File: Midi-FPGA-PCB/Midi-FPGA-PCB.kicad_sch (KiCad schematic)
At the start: 13 parts, among them Q1 DMP2123L, SW1 SW_Push, U1 ESP32-WROOM-32, U2 AP7361EA

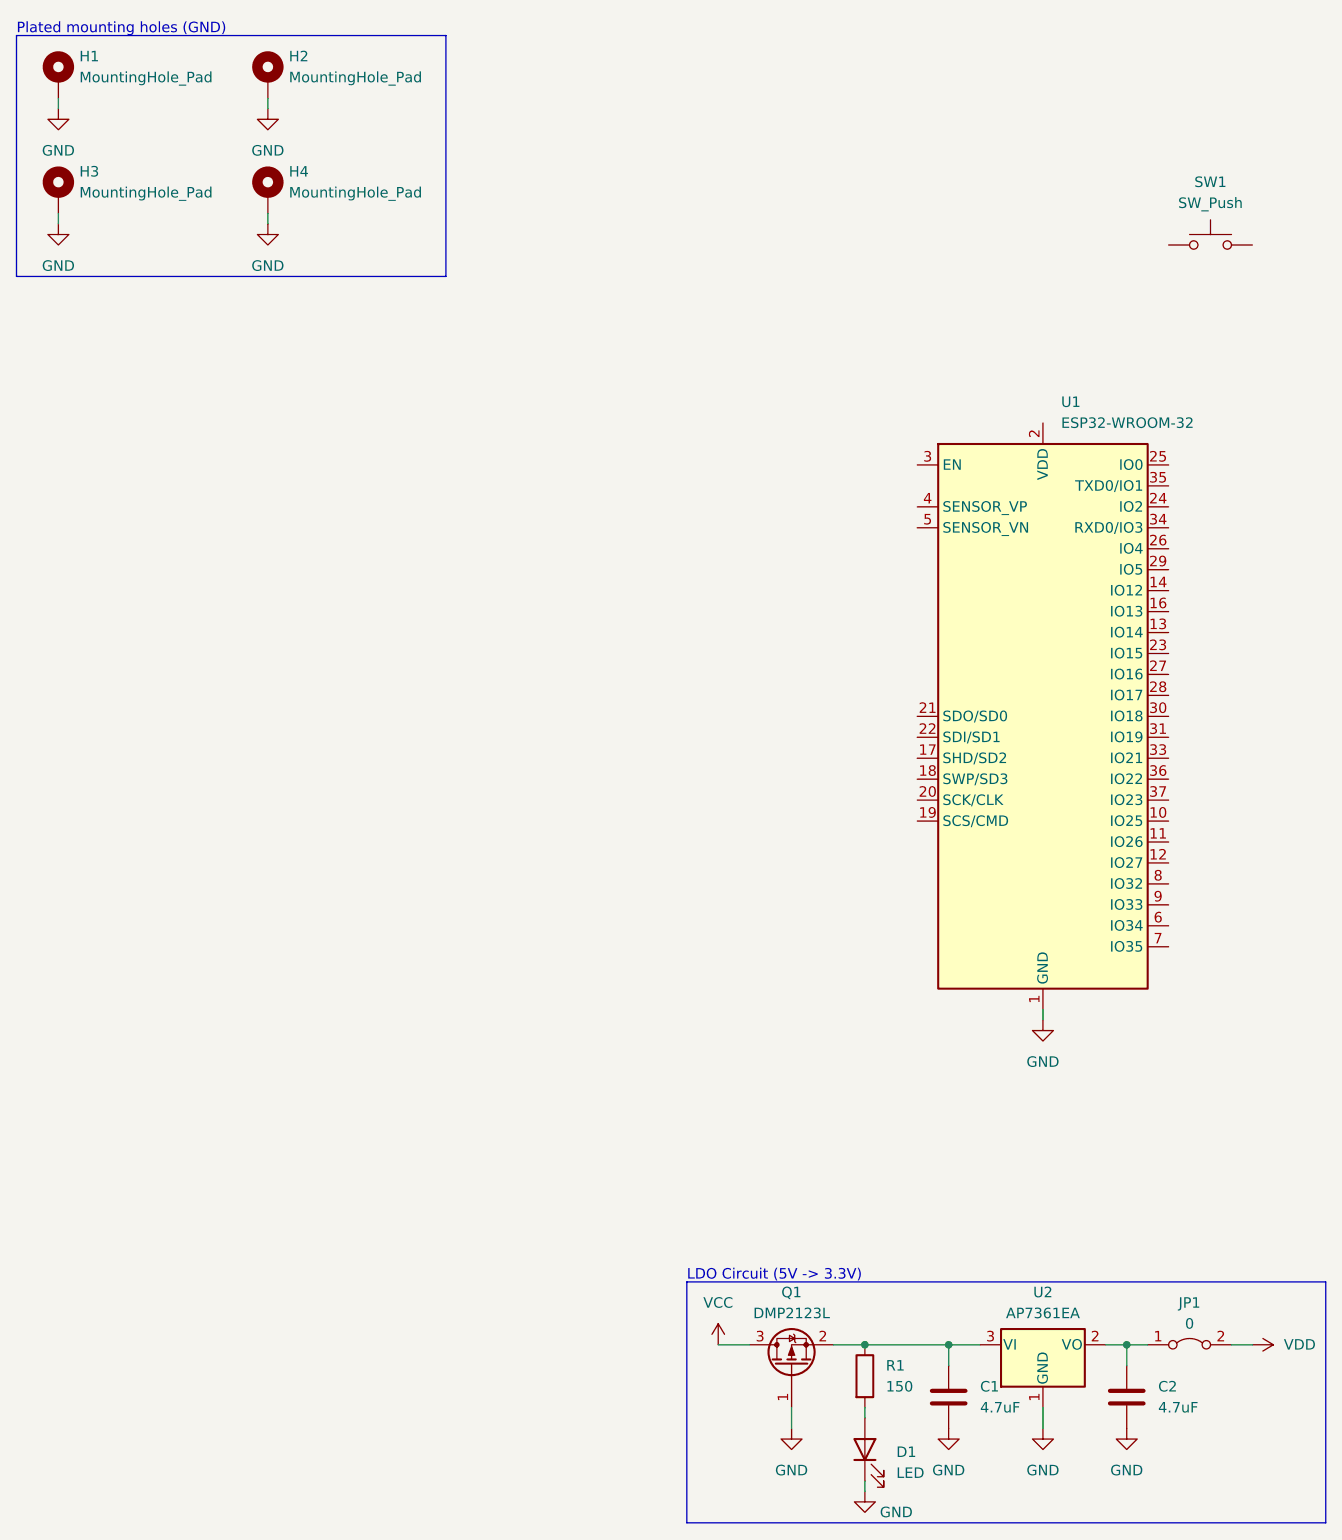
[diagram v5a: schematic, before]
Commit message: Created enable circuit
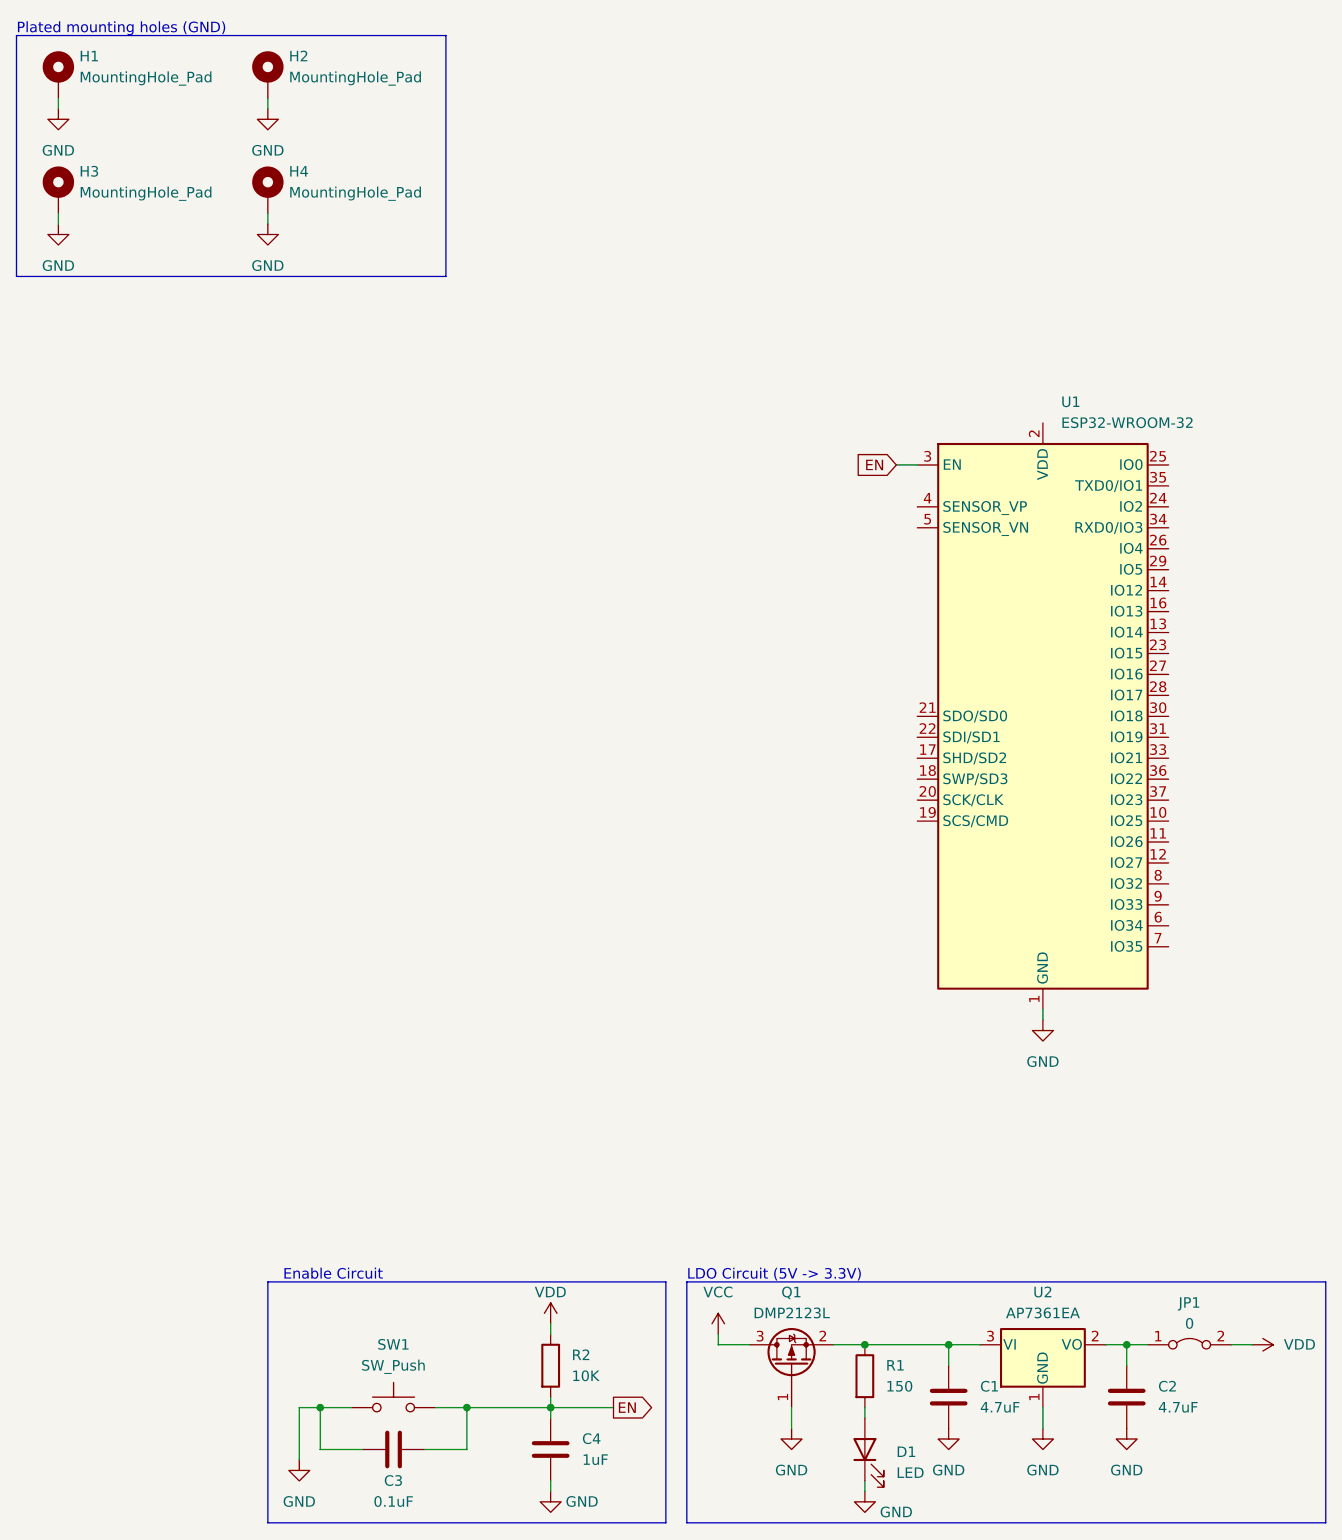
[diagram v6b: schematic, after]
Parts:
- added C3: 0.1uF, Capacitor_SMD:C_0805_2012Metric_Pad1.18x1.45mm_HandSolder, symbol Device:C
- added C4: 1uF, Capacitor_SMD:C_0805_2012Metric_Pad1.18x1.45mm_HandSolder, symbol Device:C
- added R2: 10K, Resistor_SMD:R_0805_2012Metric_Pad1.20x1.40mm_HandSolder, symbol Device:R
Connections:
- net GND: now also SW1.1, C3.1, C4.2
- net VDD: now also R2.1
- net EN: now reaches SW1.2
- net EN: now also U1.3 (EN), C3.2, C4.1, R2.2
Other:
- note added: "Enable Circuit"
- moved on the sheet: SW1

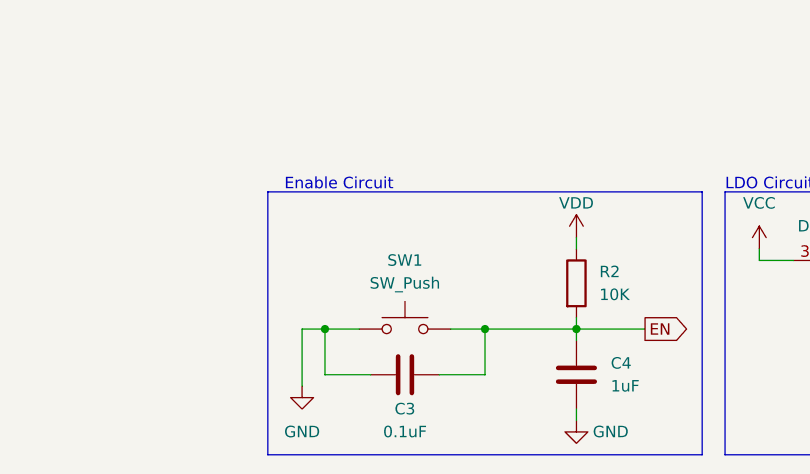
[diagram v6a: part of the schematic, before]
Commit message: Named reset switch
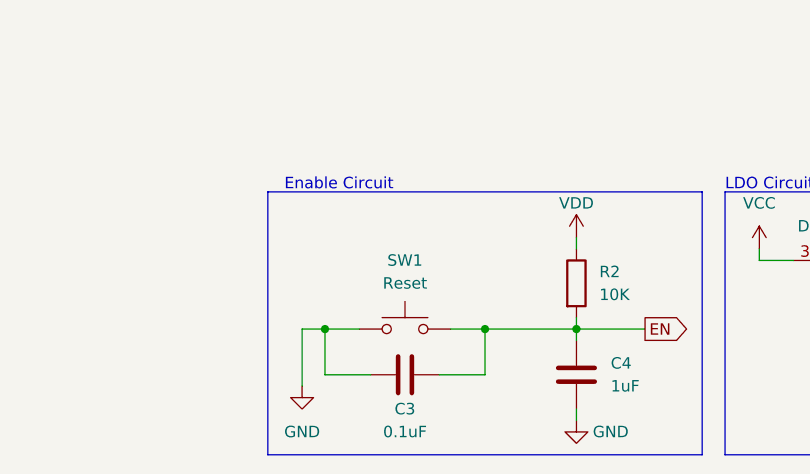
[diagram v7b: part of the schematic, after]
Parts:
- SW1: value SW_Push -> Reset
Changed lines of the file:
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@@
       (effects (font (size 1.27 1.27)))
     )
-    (property "Value" "SW_Push" (at 60.96 176.53 0)
+    (property "Value" "Reset" (at 60.96 176.53 0)
       (effects (font (size 1.27 1.27)))
     )

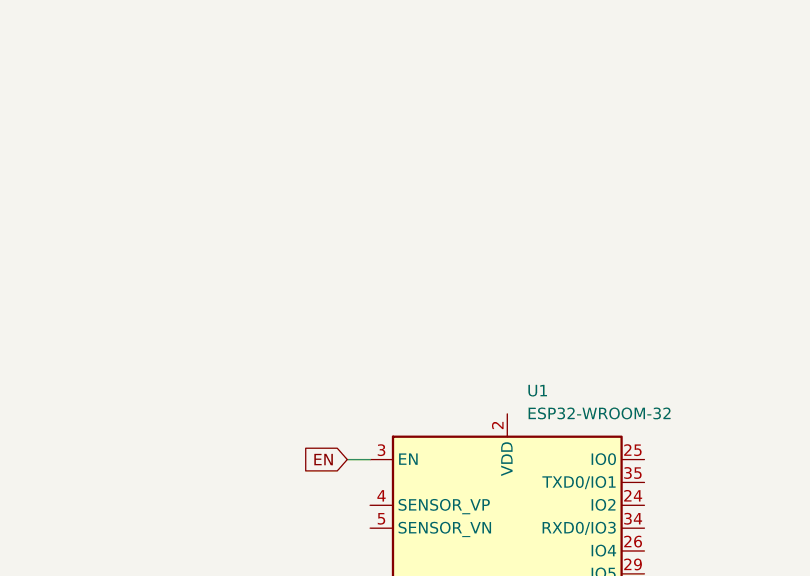
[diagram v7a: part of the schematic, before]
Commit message: Finished power and enable circuitry
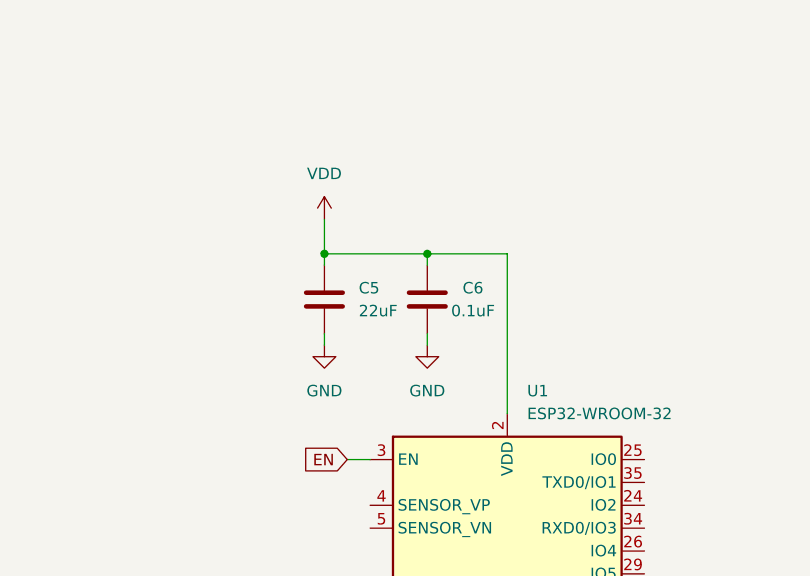
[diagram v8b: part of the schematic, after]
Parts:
- added C5: 22uF, Capacitor_SMD:C_0805_2012Metric_Pad1.18x1.45mm_HandSolder, symbol Device:C
- added C6: 0.1uF, Capacitor_SMD:C_0805_2012Metric_Pad1.18x1.45mm_HandSolder, symbol Device:C
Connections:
- net GND: now also C5.2, C6.1
- net VDD: now also U1.2 (VDD), C5.1, C6.2
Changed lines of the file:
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@@
   (junction (at 52.07 181.61) (diameter 0) (color 0 0 0 0)
   )
+  (junction (at 130.81 44.45) (diameter 0) (color 0 0 0 0)
+  )
   (junction (at 80.01 181.61) (diameter 0) (color 0 0 0 0)
   )
+  (junction (at 119.38 44.45) (diameter 0) (color 0 0 0 0)
+  )
   (junction (at 149.86 173.99) (diameter 0) (color 0 0 0 0)
   )
@@
     (stroke (width 0) (type default))
   )
+  (wire (pts (xy 119.38 44.45) (xy 130.81 44.45))
+    (stroke (width 0) (type default))
+  )
+  (wire (pts (xy 130.81 53.34) (xy 130.81 54.61))
+    (stroke (width 0) (type default))
+  )
   (wire (pts (xy 149.86 173.99) (xy 149.86 176.53))
     (stroke (width 0) (type default))
@@
     (stroke (width 0) (type default))
   )
+  (wire (pts (xy 130.81 44.45) (xy 130.81 45.72))
+    (stroke (width 0) (type default))
+  )
+  (wire (pts (xy 119.38 40.64) (xy 119.38 44.45))
+    (stroke (width 0) (type default))
+  )
   (wire (pts (xy 49.53 181.61) (xy 52.07 181.61))
     (stroke (width 0) (type default))
@@
     (stroke (width 0) (type default))
   )
+  (wire (pts (xy 119.38 53.34) (xy 119.38 54.61))
+    (stroke (width 0) (type default))
+  )
   (wire (pts (xy 80.01 190.5) (xy 80.01 191.77))
     (stroke (width 0) (type default))
@@
     (stroke (width 0) (type default))
   )
+  (wire (pts (xy 130.81 44.45) (xy 139.7 44.45))
+    (stroke (width 0) (type default))
+  )
   (wire (pts (xy 20.32 38.1) (xy 20.32 36.83))
     (stroke (width 0) (type default))
   )
+  (wire (pts (xy 139.7 44.45) (xy 139.7 62.23))
+    (stroke (width 0) (type default))
+  )
   (wire (pts (xy 114.3 173.99) (xy 118.11 173.99))
     (stroke (width 0) (type default))
@@
   )
   (wire (pts (xy 121.92 67.31) (xy 124.46 67.31))
+    (stroke (width 0) (type default))
+  )
+  (wire (pts (xy 119.38 44.45) (xy 119.38 45.72))
     (stroke (width 0) (type default))
   )
@@
     )
   )
+  (symbol (lib_id "power:GND") (at 130.81 54.61 0) (unit 1)
+    (in_bom yes) (on_board yes) (dnp no) (fields_autoplaced)
+    (property "Reference" "#PWR018" (at 130.81 60.96 0)
+      (effects (font (size 1.27 1.27)) hide)
+    )
+    (property "Value" "GND" (at 130.81 59.69 0)
+      (effects (font (size 1.27 1.27)))
+    )
+    (property "Footprint" "" (at 130.81 54.61 0)
+      (effects (font (size 1.27 1.27)) hide)
+    )
+    (property "Datasheet" "" (at 130.81 54.61 0)
+      (effects (font (size 1.27 1.27)) hide)
+    )
+    (pin "1")
+    (instances
+      (project "Midi-FPGA-PCB"
+        (path "/75ad38e9-b0d3-45bc-bcac-026c9800f4ea"
+          (reference "#PWR018") (unit 1)
+        )
+      )
+    )
+  )
   (symbol (lib_id "Device:C") (at 60.96 186.69 90) (unit 1)
     (in_bom yes) (on_board yes) (dnp no)
@@
         (path "/75ad38e9-b0d3-45bc-bcac-026c9800f4ea"
           (reference "#PWR08") (unit 1)
+        )
+      )
+    )
+  )
+  (symbol (lib_id "power:GND") (at 119.38 54.61 0) (unit 1)
+    (in_bom yes) (on_board yes) (dnp no) (fields_autoplaced)
+    (property "Reference" "#PWR017" (at 119.38 60.96 0)
+      (effects (font (size 1.27 1.27)) hide)
+    )
+    (property "Value" "GND" (at 119.38 59.69 0)
+      (effects (font (size 1.27 1.27)))
+    )
+    (property "Footprint" "" (at 119.38 54.61 0)
+      (effects (font (size 1.27 1.27)) hide)
+    )
+    (property "Datasheet" "" (at 119.38 54.61 0)
+      (effects (font (size 1.27 1.27)) hide)
+    )
+    (pin "1")
+    (instances
+      (project "Midi-FPGA-PCB"
+        (path "/75ad38e9-b0d3-45bc-bcac-026c9800f4ea"
+          (reference "#PWR017") (unit 1)
         )
       )
@@
     )
   )
+  (symbol (lib_id "power:VDD") (at 119.38 40.64 0) (unit 1)
+    (in_bom yes) (on_board yes) (dnp no) (fields_autoplaced)
+    (property "Reference" "#PWR016" (at 119.38 44.45 0)
+      (effects (font (size 1.27 1.27)) hide)
+    )
+    (property "Value" "VDD" (at 119.38 35.56 0)
+      (effects (font (size 1.27 1.27)))
+    )
+    (property "Footprint" "" (at 119.38 40.64 0)
+      (effects (font (size 1.27 1.27)) hide)
+    )
+    (property "Datasheet" "" (at 119.38 40.64 0)
+      (effects (font (size 1.27 1.27)) hide)
+    )
+    (pin "1")
+    (instances
+      (project "Midi-FPGA-PCB"
+        (path "/75ad38e9-b0d3-45bc-bcac-026c9800f4ea"
+          (reference "#PWR016") (unit 1)
+        )
+      )
+    )
+  )
   (symbol (lib_id "Device:Q_PMOS_GSD") (at 109.22 176.53 90) (unit 1)
     (in_bom yes) (on_board yes) (dnp no) (fields_autoplaced)
@@
     )
   )
+  (symbol (lib_id "Device:C") (at 119.38 49.53 0) (unit 1)
+    (in_bom yes) (on_board yes) (dnp no) (fields_autoplaced)
+    (property "Reference" "C5" (at 123.19 48.26 0)
+      (effects (font (size 1.27 1.27)) (justify left))
+    )
+    (property "Value" "22uF" (at 123.19 50.8 0)
+      (effects (font (size 1.27 1.27)) (justify left))
+    )
+    (property "Footprint" "Capacitor_SMD:C_0805_2012Metric_Pad1.18x1.45mm_HandSolder" (at 120.3452 53.34 0)
+      (effects (font (size 1.27 1.27)) hide)
+    )
+    (property "Datasheet" "https://search.murata.co.jp/Ceramy/image/img/A01X/G101/ENG/GRM21BZ71A226ME15-01.pdf" (at 119.38 49.53 0)
+      (effects (font (size 1.27 1.27)) hide)
+    )
+    (property "URL" "https://www.digikey.co.uk/en/products/detail/murata-electronics/GRM21BZ71A226ME15L/13904953" (at 119.38 49.53 0)
+      (effects (font (size 1.27 1.27)) hide)
+    )
+    (pin "1")
+    (pin "2")
+    (instances
+      (project "Midi-FPGA-PCB"
+        (path "/75ad38e9-b0d3-45bc-bcac-026c9800f4ea"
+          (reference "C5") (unit 1)
+        )
+      )
+    )
+  )
   (symbol (lib_id "Device:C") (at 128.27 180.34 0) (unit 1)
     (in_bom yes) (on_board yes) (dnp no)
@@
         )
       )
+    )
+  )
+  (symbol (lib_id "Device:C") (at 130.81 49.53 180) (unit 1)
+    (in_bom yes) (on_board yes) (dnp no)
+    (property "Reference" "C6" (at 135.89 48.26 0)
+      (effects (font (size 1.27 1.27)))
+    )
+    (property "Value" "0.1uF" (at 135.89 50.8 0)
+      (effects (font (size 1.27 1.27)))
+    )
+    (property "Footprint" "Capacitor_SMD:C_0805_2012Metric_Pad1.18x1.45mm_HandSolder" (at 129.8448 45.72 0)
+      (effects (font (size 1.27 1.27)) hide)
+    )
+    (property "Datasheet" "https://mm.digikey.com/Volume0/opasdata/d220001/medias/docus/609/CL21B104KBCNNN_Spec.pdf" (at 130.81 49.53 0)
+      (effects (font (size 1.27 1.27)) hide)
+    )
+    (property "URL" "https://www.digikey.co.uk/en/products/detail/samsung-electro-mechanics/CL21B104KBCNNNC/3886661" (at 130.81 49.53 90)
+      (effects (font (size 1.27 1.27)) hide)
+    )
+    (pin "1")
+    (pin "2")
+    (instances
+      (project "Midi-FPGA-PCB"
+        (path "/75ad38e9-b0d3-45bc-bcac-026c9800f4ea"
+          (reference "C6") (unit 1)
+        )
+      )
